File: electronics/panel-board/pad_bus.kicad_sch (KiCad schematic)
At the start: 7 parts, among them J13 Conn_02x04_Odd_Even, J14 Conn_02x04_Odd_Even, U10 TJA1042T-3

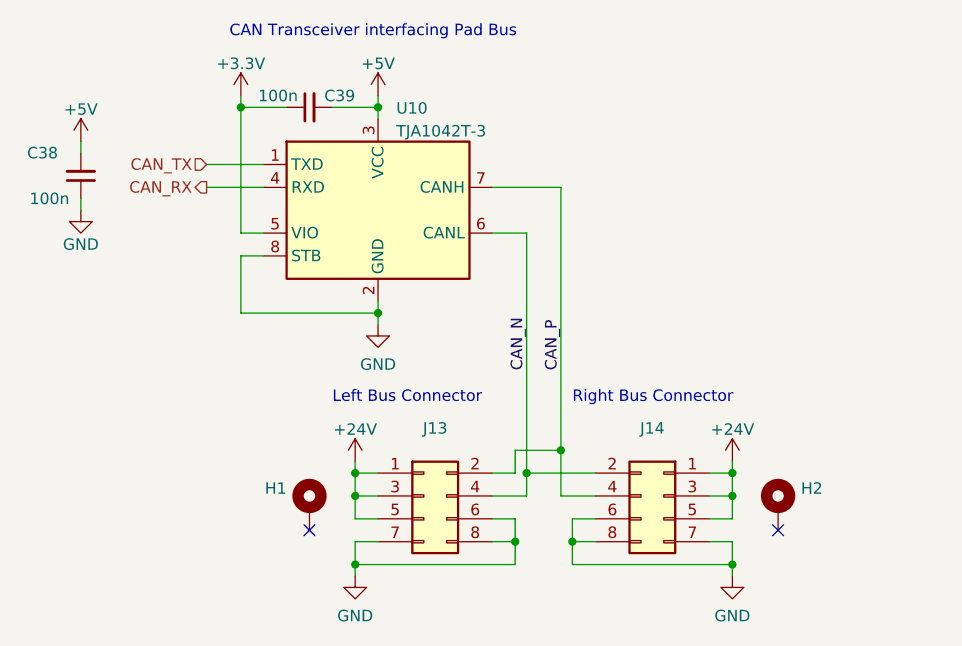
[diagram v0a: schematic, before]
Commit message: Update PadBUS standard
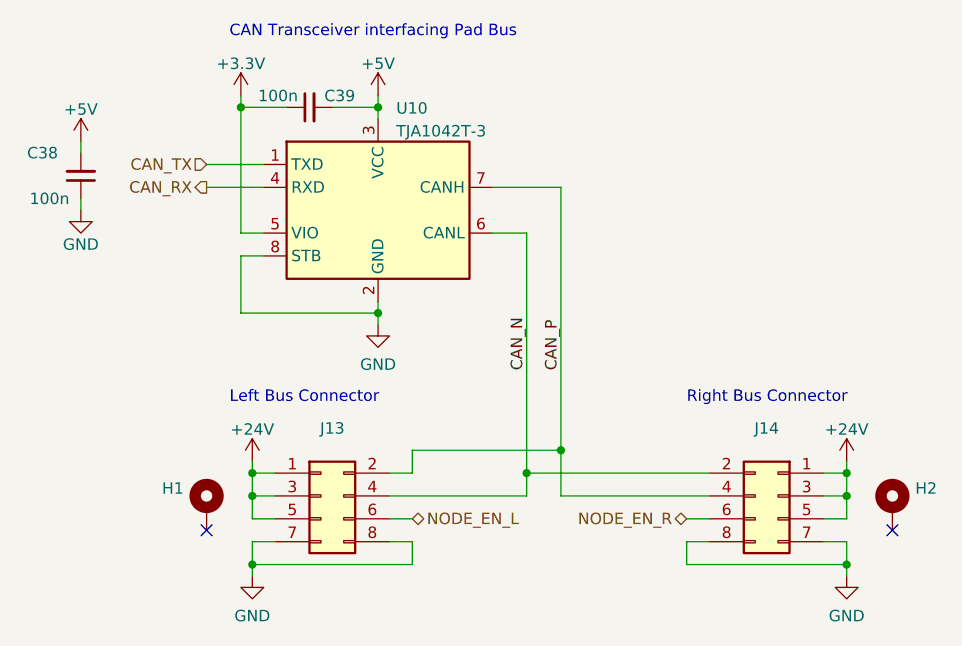
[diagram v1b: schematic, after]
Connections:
- net GND: no longer J13.6 (Pin_6), J14.6 (Pin_6)
- new net NODE_EN_L: J13.6 (Pin_6)
- new net NODE_EN_R: J14.6 (Pin_6)
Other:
- moved on the sheet: H1, H2, J13, J14

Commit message: Add node termination
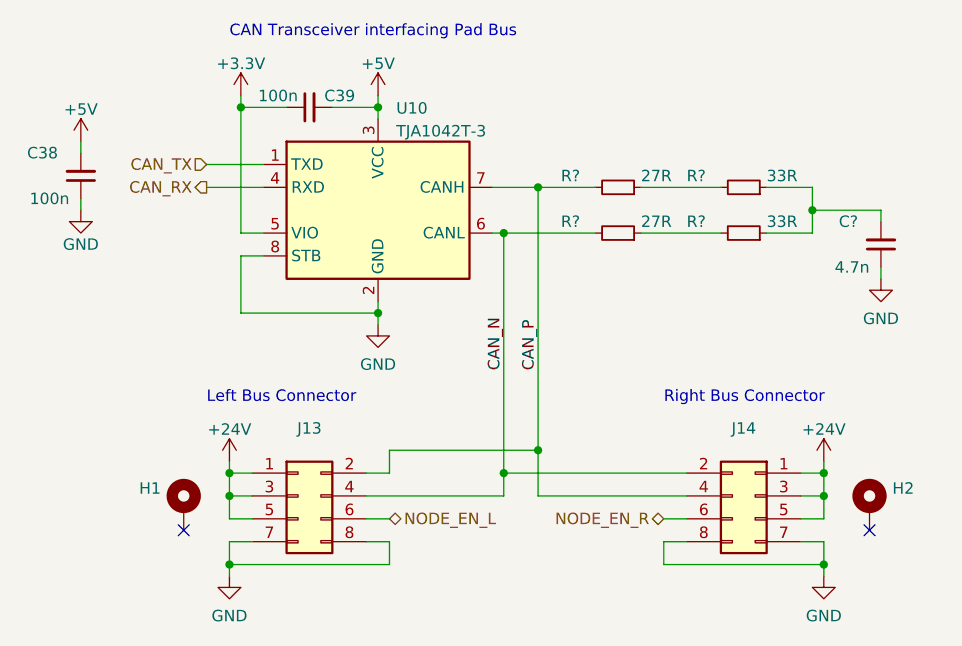
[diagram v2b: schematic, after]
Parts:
- added C?: 4.7n, Capacitor_SMD:C_0603_1608Metric, symbol Device:C_Small
- added R? (x2): 33R, Resistor_SMD:R_0603_1608Metric, symbol Device:R_Small
- added R? (x2): 27R, Resistor_SMD:R_0603_1608Metric, symbol Device:R_Small
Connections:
- net CAN_N: now also R?.2
- net CAN_P: now also R?.2
- net GND: now also C?.1
- new net: C?.2, R?.1, R?.1
- new net: R?.1, R?.2 (x2)
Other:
- moved on the sheet: H1, H2, J13, J14

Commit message: Actually update the schematic references
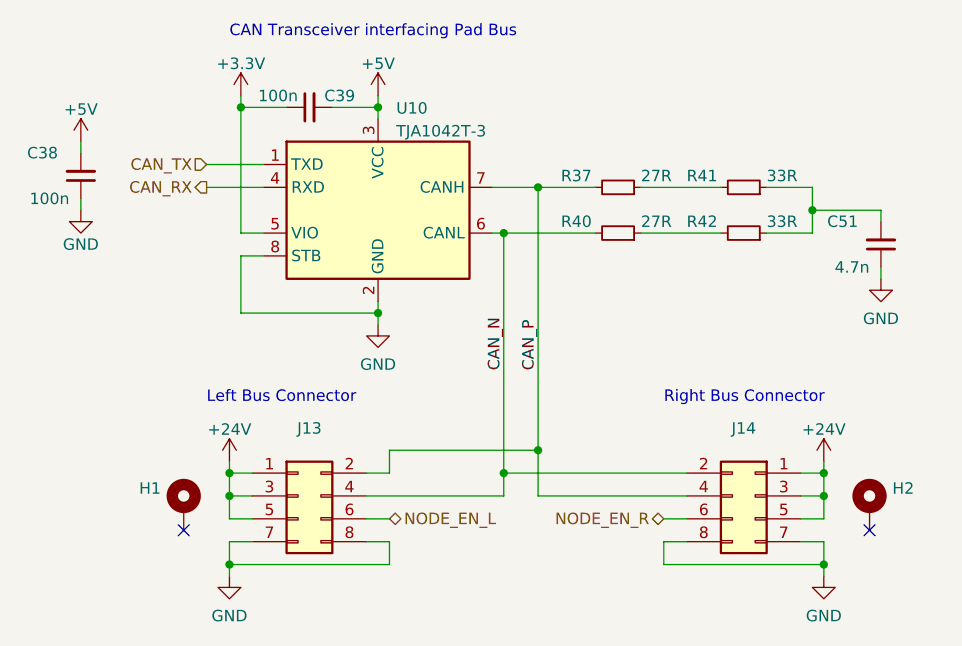
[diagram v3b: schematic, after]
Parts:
- gave numbers to parts that had none: 5
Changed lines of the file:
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@@
   (symbol (lib_id "Device:C_Small") (at 113.03 43.18 180) (unit 1)
     (in_bom yes) (on_board yes)
-    (property "Reference" "C?" (id 0) (at 110.49 40.64 0)
+    (property "Reference" "C51" (id 0) (at 110.49 40.64 0)
       (effects (font (size 1.27 1.27)) (justify left))
     )
@@
   (symbol (lib_id "Device:R_Small") (at 97.79 36.83 270) (mirror x) (unit 1)
     (in_bom yes) (on_board yes)
-    (property "Reference" "R?" (id 0) (at 91.44 35.56 90)
+    (property "Reference" "R41" (id 0) (at 91.44 35.56 90)
       (effects (font (size 1.27 1.27)) (justify left))
     )
@@
   (symbol (lib_id "power:GND") (at 113.03 46.99 0) (unit 1)
     (in_bom yes) (on_board yes)
-    (property "Reference" "#PWR?" (id 0) (at 113.03 53.34 0)
+    (property "Reference" "#PWR0123" (id 0) (at 113.03 53.34 0)
       (effects (font (size 1.27 1.27)) hide)
     )
@@
   (symbol (lib_id "Device:R_Small") (at 83.82 36.83 270) (mirror x) (unit 1)
     (in_bom yes) (on_board yes)
-    (property "Reference" "R?" (id 0) (at 77.47 35.56 90)
+    (property "Reference" "R37" (id 0) (at 77.47 35.56 90)
       (effects (font (size 1.27 1.27)) (justify left))
     )
@@
   (symbol (lib_id "Device:R_Small") (at 97.79 41.91 270) (mirror x) (unit 1)
     (in_bom yes) (on_board yes)
-    (property "Reference" "R?" (id 0) (at 91.44 40.64 90)
+    (property "Reference" "R42" (id 0) (at 91.44 40.64 90)
       (effects (font (size 1.27 1.27)) (justify left))
     )
@@
   (symbol (lib_id "Device:R_Small") (at 83.82 41.91 270) (mirror x) (unit 1)
     (in_bom yes) (on_board yes)
-    (property "Reference" "R?" (id 0) (at 77.47 40.64 90)
-      (effects (font (size 1.27 1.27)) (justify left))
-    )
+    (property "Reference" "R40" (id 0) (at 77.47 40.64 90)
+      (effects (font (size 1.27 1.27)) (justify left))
+    )

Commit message: Pre LED grid changes
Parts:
- removed C51: 4.7n, Capacitor_SMD:C_0603_1608Metric, symbol Device:C_Small
- removed R37, R40: 27R, Resistor_SMD:R_0603_1608Metric, symbol Device:R_Small
- removed R41, R42: 33R, Resistor_SMD:R_0603_1608Metric, symbol Device:R_Small
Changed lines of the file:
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@@
   (junction (at 40.64 68.58) (diameter 0) (color 0 0 0 0)
   )
-  (junction (at 74.93 36.83) (diameter 0) (color 0 0 0 0)
-  )
   (junction (at 57.15 27.94) (diameter 0) (color 0 0 0 0)
   )
@@
   (junction (at 106.68 78.74) (diameter 0) (color 0 0 0 0)
   )
-  (junction (at 71.12 41.91) (diameter 0) (color 0 0 0 0)
-  )
   (junction (at 40.64 78.74) (diameter 0) (color 0 0 0 0)
   )
@@
   )
   (junction (at 106.68 68.58) (diameter 0) (color 0 0 0 0)
-  )
-  (junction (at 105.41 39.37) (diameter 0) (color 0 0 0 0)
   )
   (no_connect (at 35.56 74.93))
@@
     (stroke (width 0) (type default) (color 0 0 0 0))
   )
-  (wire (pts (xy 74.93 36.83) (xy 81.28 36.83))
-    (stroke (width 0) (type default) (color 0 0 0 0))
-  )
   (wire (pts (xy 74.93 66.04) (xy 74.93 71.12))
     (stroke (width 0) (type default) (color 0 0 0 0))
@@
     (stroke (width 0) (type default) (color 0 0 0 0))
   )
-  (wire (pts (xy 86.36 41.91) (xy 95.25 41.91))
-    (stroke (width 0) (type default) (color 0 0 0 0))
-  )
   (wire (pts (xy 41.91 27.94) (xy 41.91 41.91))
     (stroke (width 0) (type default) (color 0 0 0 0))
@@
     (stroke (width 0) (type default) (color 0 0 0 0))
   )
-  (wire (pts (xy 105.41 41.91) (xy 105.41 39.37))
-    (stroke (width 0) (type default) (color 0 0 0 0))
-  )
   (wire (pts (xy 106.68 76.2) (xy 104.14 76.2))
     (stroke (width 0) (type default) (color 0 0 0 0))
   )
-  (wire (pts (xy 86.36 36.83) (xy 95.25 36.83))
-    (stroke (width 0) (type default) (color 0 0 0 0))
-  )
   (wire (pts (xy 58.42 78.74) (xy 58.42 76.2))
     (stroke (width 0) (type default) (color 0 0 0 0))
@@
     (stroke (width 0) (type default) (color 0 0 0 0))
   )
-  (wire (pts (xy 113.03 39.37) (xy 105.41 39.37))
-    (stroke (width 0) (type default) (color 0 0 0 0))
-  )
-  (wire (pts (xy 113.03 45.72) (xy 113.03 46.99))
-    (stroke (width 0) (type default) (color 0 0 0 0))
-  )
   (wire (pts (xy 57.15 52.07) (xy 57.15 50.8))
     (stroke (width 0) (type default) (color 0 0 0 0))
@@
     (stroke (width 0) (type default) (color 0 0 0 0))
   )
-  (wire (pts (xy 100.33 41.91) (xy 105.41 41.91))
-    (stroke (width 0) (type default) (color 0 0 0 0))
-  )
-  (wire (pts (xy 105.41 39.37) (xy 105.41 36.83))
-    (stroke (width 0) (type default) (color 0 0 0 0))
-  )
   (wire (pts (xy 57.15 27.94) (xy 57.15 29.21))
     (stroke (width 0) (type default) (color 0 0 0 0))
@@
     (stroke (width 0) (type default) (color 0 0 0 0))
   )
-  (wire (pts (xy 105.41 36.83) (xy 100.33 36.83))
-    (stroke (width 0) (type default) (color 0 0 0 0))
-  )
   (wire (pts (xy 58.42 76.2) (xy 55.88 76.2))
     (stroke (width 0) (type default) (color 0 0 0 0))
@@
     (stroke (width 0) (type default) (color 0 0 0 0))
   )
-  (wire (pts (xy 113.03 40.64) (xy 113.03 39.37))
-    (stroke (width 0) (type default) (color 0 0 0 0))
-  )
   (wire (pts (xy 41.91 27.94) (xy 46.99 27.94))
     (stroke (width 0) (type default) (color 0 0 0 0))
@@
   )
   (wire (pts (xy 74.93 71.12) (xy 91.44 71.12))
-    (stroke (width 0) (type default) (color 0 0 0 0))
-  )
-  (wire (pts (xy 71.12 41.91) (xy 81.28 41.91))
     (stroke (width 0) (type default) (color 0 0 0 0))
   )
@@
   (hierarchical_label "CAN_RX" (shape output) (at 38.1 36.83 180)
     (effects (font (size 1.27 1.27)) (justify right))
-  )
-  (symbol (lib_id "Device:C_Small") (at 113.03 43.18 180) (unit 1)
-    (in_bom yes) (on_board yes)
-    (property "Reference" "C51" (id 0) (at 110.49 40.64 0)
-      (effects (font (size 1.27 1.27)) (justify left))
-    )
-    (property "Value" "4.7n" (id 1) (at 111.76 45.72 0)
-      (effects (font (size 1.27 1.27)) (justify left))
-    )
-    (property "Footprint" "Capacitor_SMD:C_0603_1608Metric" (id 2) (at 113.03 43.18 0)
-      (effects (font (size 1.27 1.27)) hide)
-    )
-    (property "Datasheet" "~" (id 3) (at 113.03 43.18 0)
-      (effects (font (size 1.27 1.27)) hide)
-    )
-    (pin "1")
-    (pin "2")
   )
   (symbol (lib_id "power:+24V") (at 40.64 67.31 0) (unit 1)
@@
     )
     (property "Datasheet" "~" (id 3) (at 24.13 35.56 0)
-      (effects (font (size 1.27 1.27)) hide)
-    )
-    (pin "1")
-    (pin "2")
-  )
-  (symbol (lib_id "Device:R_Small") (at 97.79 36.83 270) (mirror x) (unit 1)
-    (in_bom yes) (on_board yes)
-    (property "Reference" "R41" (id 0) (at 91.44 35.56 90)
-      (effects (font (size 1.27 1.27)) (justify left))
-    )
-    (property "Value" "33R" (id 1) (at 100.33 35.56 90)
-      (effects (font (size 1.27 1.27)) (justify left))
-    )
-    (property "Footprint" "Resistor_SMD:R_0603_1608Metric" (id 2) (at 97.79 36.83 0)
-      (effects (font (size 1.27 1.27)) hide)
-    )
-    (property "Datasheet" "~" (id 3) (at 97.79 36.83 0)
       (effects (font (size 1.27 1.27)) hide)
     )
@@
     (pin "8")
   )
-  (symbol (lib_id "power:GND") (at 113.03 46.99 0) (unit 1)
-    (in_bom yes) (on_board yes)
-    (property "Reference" "#PWR0123" (id 0) (at 113.03 53.34 0)
-      (effects (font (size 1.27 1.27)) hide)
-    )
-    (property "Value" "GND" (id 1) (at 113.03 51.4334 0))
-    (property "Footprint" "" (id 2) (at 113.03 46.99 0)
-      (effects (font (size 1.27 1.27)) hide)
-    )
-    (property "Datasheet" "" (id 3) (at 113.03 46.99 0)
-      (effects (font (size 1.27 1.27)) hide)
-    )
-    (pin "1")
-  )
   (symbol (lib_id "power:+5V") (at 24.13 31.75 0) (unit 1)
     (in_bom yes) (on_board yes) (fields_autoplaced)
@@
     )
     (pin "1")
-  )
-  (symbol (lib_id "Device:R_Small") (at 83.82 36.83 270) (mirror x) (unit 1)
-    (in_bom yes) (on_board yes)
-    (property "Reference" "R37" (id 0) (at 77.47 35.56 90)
-      (effects (font (size 1.27 1.27)) (justify left))
-    )
-    (property "Value" "27R" (id 1) (at 86.36 35.56 90)
-      (effects (font (size 1.27 1.27)) (justify left))
-    )
-    (property "Footprint" "Resistor_SMD:R_0603_1608Metric" (id 2) (at 83.82 36.83 0)
-      (effects (font (size 1.27 1.27)) hide)
-    )
-    (property "Datasheet" "~" (id 3) (at 83.82 36.83 0)
-      (effects (font (size 1.27 1.27)) hide)
-    )
-    (pin "1")
-    (pin "2")
   )
   (symbol (lib_id "power:GND") (at 106.68 80.01 0) (mirror y) (unit 1)
@@
     (pin "8")
   )
-  (symbol (lib_id "Device:R_Small") (at 97.79 41.91 270) (mirror x) (unit 1)
-    (in_bom yes) (on_board yes)
-    (property "Reference" "R42" (id 0) (at 91.44 40.64 90)
-      (effects (font (size 1.27 1.27)) (justify left))
-    )
-    (property "Value" "33R" (id 1) (at 100.33 40.64 90)
-      (effects (font (size 1.27 1.27)) (justify left))
-    )
-    (property "Footprint" "Resistor_SMD:R_0603_1608Metric" (id 2) (at 97.79 41.91 0)
-      (effects (font (size 1.27 1.27)) hide)
-    )
-    (property "Datasheet" "~" (id 3) (at 97.79 41.91 0)
-      (effects (font (size 1.27 1.27)) hide)
-    )
-    (pin "1")
-    (pin "2")
-  )
   (symbol (lib_id "power:+3.3V") (at 41.91 26.67 0) (unit 1)
     (in_bom yes) (on_board yes) (fields_autoplaced)
@@
     (pin "1")
   )
-  (symbol (lib_id "Device:R_Small") (at 83.82 41.91 270) (mirror x) (unit 1)
-    (in_bom yes) (on_board yes)
-    (property "Reference" "R40" (id 0) (at 77.47 40.64 90)
-      (effects (font (size 1.27 1.27)) (justify left))
-    )
-    (property "Value" "27R" (id 1) (at 86.36 40.64 90)
-      (effects (font (size 1.27 1.27)) (justify left))
-    )
-    (property "Footprint" "Resistor_SMD:R_0603_1608Metric" (id 2) (at 83.82 41.91 0)
-      (effects (font (size 1.27 1.27)) hide)
-    )
-    (property "Datasheet" "~" (id 3) (at 83.82 41.91 0)
-      (effects (font (size 1.27 1.27)) hide)
-    )
-    (pin "1")
-    (pin "2")
-  )
   (symbol (lib_id "Device:C_Small") (at 49.53 27.94 90) (unit 1)
